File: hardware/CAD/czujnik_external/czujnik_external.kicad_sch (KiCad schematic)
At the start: 4 parts, among them J1 8P8C, J2 PMS5003 socket, J3 DHT22 socket, J4 ADC socket

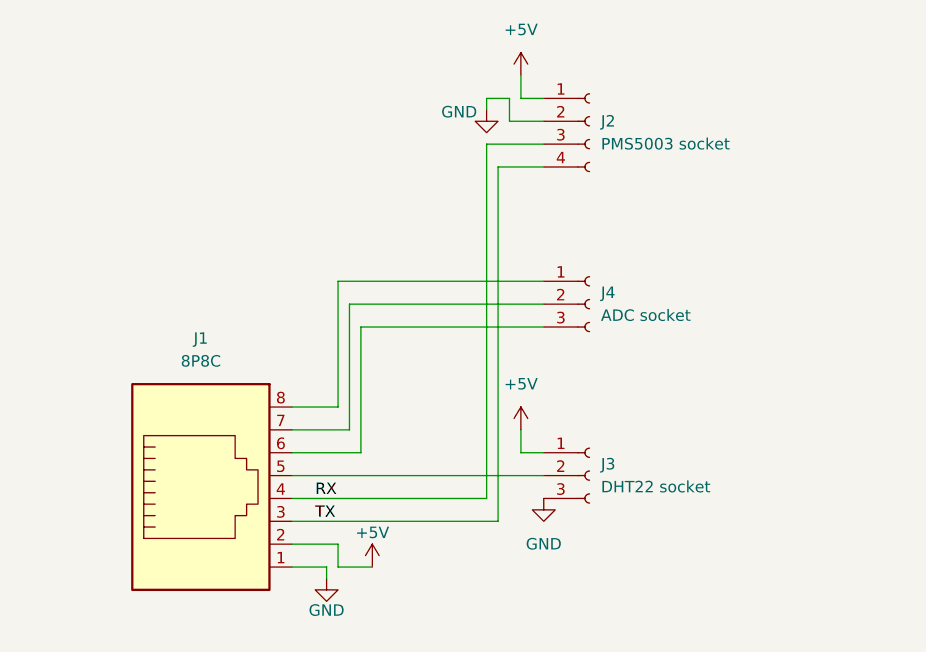
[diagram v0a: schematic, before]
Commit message: refactor PCBs, add gerber files
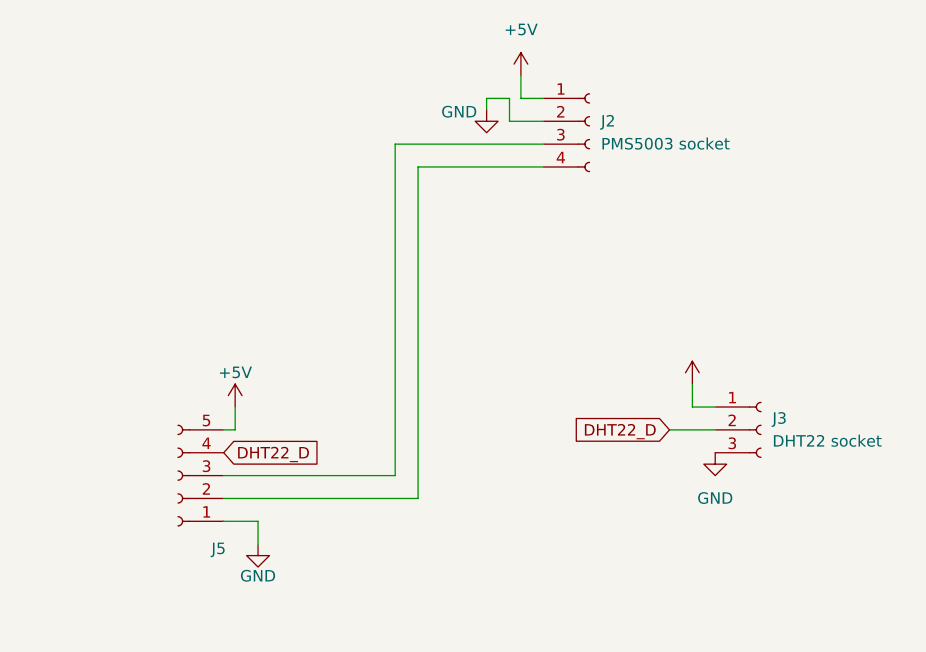
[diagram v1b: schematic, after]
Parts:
- removed J1: 8P8C, Connector_RJ:RJ45_Connfly_DS1128-09-S8xx-S_Horizontal, symbol Connector:8P8C
- removed J4: ADC socket, Connector_PinSocket_2.54mm:PinSocket_1x03_P2.54mm_Vertical, symbol Connector:Conn_01x03_Socket
- added J5: Conn_01x05_Socket, Connector_PinSocket_2.54mm:PinSocket_1x05_P2.54mm_Vertical, symbol Connector:Conn_01x05_Socket
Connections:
- net +5V: now also J5.5 (Pin_5)
- net GND: now also J5.1 (Pin_1)
- net DHT22_D: now reaches J3.2 (Pin_2)
- net DHT22_D: now also J5.4 (Pin_4)
- net RX: no longer names the net of J2.3 (Pin_3)
- net RX: now also J5.3 (Pin_3)
- net TX: no longer names the net of J2.4 (Pin_4)
- net TX: now also J5.2 (Pin_2)
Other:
- moved on the sheet: J3

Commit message: add DB9 connectors to PCBs
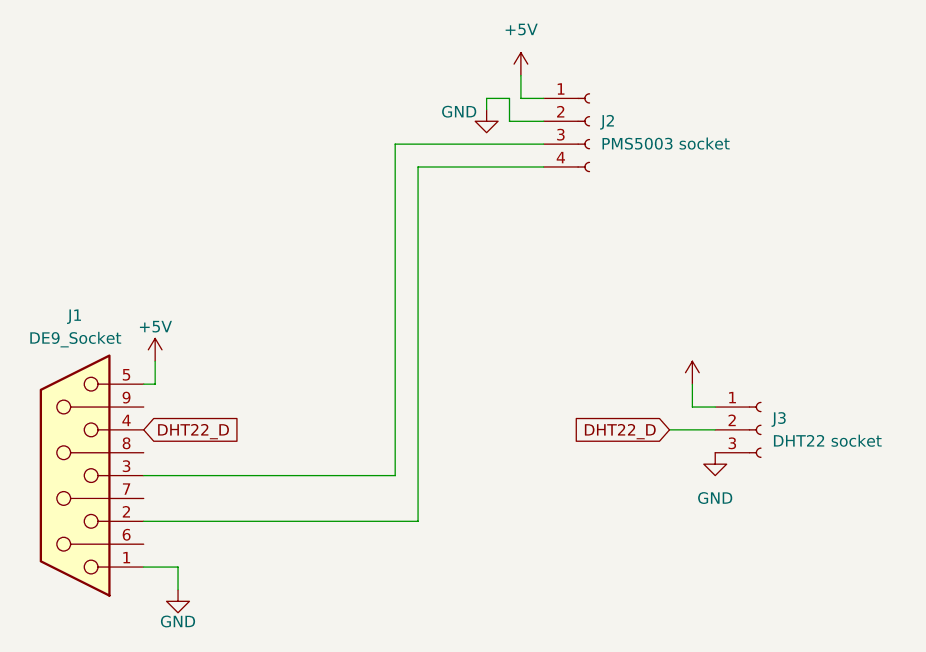
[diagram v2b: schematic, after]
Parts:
- removed J5: Conn_01x05_Socket, Connector_PinSocket_2.54mm:PinSocket_1x05_P2.54mm_Vertical, symbol Connector:Conn_01x05_Socket
- added J1: DE9_Socket, Connector_Dsub:DSUB-9_Socket_Horizontal_P2.77x2.54mm_EdgePinOffset9.40mm, symbol Connector:DE9_Socket
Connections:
- net +5V: now also J1.5
- net DHT22_D: now also J1.4
- net GND: now also J1.1
- net at J2.3 (Pin_3): now also J1.3
- net at J2.4 (Pin_4): now also J1.2
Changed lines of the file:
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@@
 	(wire
 		(pts
-			(xy 154.94 77.47) (xy 154.94 80.01)
-		)
-		(stroke
-			(width 0)
-			(type default)
-		)
-	)
-	(wire
-		(pts
-			(xy 151.13 74.93) (xy 172.72 74.93)
+			(xy 146.05 82.55) (xy 146.05 85.09)
+		)
+		(stroke
+			(width 0)
+			(type default)
+		)
+	)
+	(wire
+		(pts
+			(xy 142.24 72.39) (xy 170.18 72.39)
 		)
 		(stroke
@@
 	(wire
 		(pts
+			(xy 172.72 77.47) (xy 142.24 77.47)
+		)
+		(stroke
+			(width 0)
+			(type default)
+		)
+	)
+	(wire
+		(pts
 			(xy 182.88 30.48) (xy 180.34 30.48)
 		)
@@
 	(wire
 		(pts
-			(xy 152.4 67.31) (xy 151.13 67.31)
+			(xy 143.51 62.23) (xy 142.24 62.23)
 		)
 		(stroke
@@
 	(wire
 		(pts
-			(xy 151.13 77.47) (xy 154.94 77.47)
+			(xy 142.24 82.55) (xy 146.05 82.55)
 		)
 		(stroke
@@
 	(wire
 		(pts
-			(xy 172.72 74.93) (xy 172.72 38.1)
+			(xy 172.72 38.1) (xy 172.72 77.47)
 		)
 		(stroke
@@
 	(wire
 		(pts
-			(xy 152.4 64.77) (xy 152.4 67.31)
+			(xy 143.51 59.69) (xy 143.51 62.23)
 		)
 		(stroke
@@
 		(pts
 			(xy 186.69 30.48) (xy 184.15 30.48)
-		)
-		(stroke
-			(width 0)
-			(type default)
-		)
-	)
-	(wire
-		(pts
-			(xy 170.18 72.39) (xy 151.13 72.39)
 		)
 		(stroke
@@
 	(global_label "DHT22_D"
 		(shape input)
-		(at 151.13 69.85 0)
+		(at 142.24 67.31 0)
 		(fields_autoplaced yes)
 		(effects
@@
 		)
 		(property "Intersheetrefs" "${INTERSHEET_REFS}"
-			(at 162.3399 69.85 0)
+			(at 153.4499 67.31 0)
 			(effects
 				(font
@@
 		)
 		(property "Netclass" ""
-			(at 151.13 72.0408 0)
+			(at 142.24 69.5008 0)
 			(effects
 				(font
@@
 	)
 	(symbol
-		(lib_id "Connector:Conn_01x05_Socket")
-		(at 146.05 72.39 180)
-		(unit 1)
-		(exclude_from_sim no)
-		(in_bom yes)
-		(on_board yes)
-		(dnp no)
-		(property "Reference" "J5"
-			(at 151.384 80.518 0)
-			(effects
-				(font
-					(size 1.27 1.27)
-				)
-				(justify left)
-			)
-		)
-		(property "Value" "Conn_01x05_Socket"
-			(at 156.21 80.01 0)
-			(effects
-				(font
-					(size 1.27 1.27)
-				)
-				(justify left)
-				(hide yes)
-			)
-		)
-		(property "Footprint" "Connector_PinSocket_2.54mm:PinSocket_1x05_P2.54mm_Vertical"
-			(at 146.05 72.39 0)
-			(effects
-				(font
-					(size 1.27 1.27)
-				)
-				(hide yes)
-			)
-		)
-		(property "Datasheet" "~"
-			(at 146.05 72.39 0)
-			(effects
-				(font
-					(size 1.27 1.27)
-				)
-				(hide yes)
-			)
-		)
-		(property "Description" "Generic connector, single row, 01x05, script generated"
-			(at 146.05 72.39 0)
-			(effects
-				(font
-					(size 1.27 1.27)
-				)
-				(hide yes)
-			)
-		)
-		(pin "1"
-		)
-		(pin "3"
-		)
-		(pin "5"
-		)
-		(pin "2"
-		)
-		(pin "4"
-		)
-		(instances
-			(project ""
-				(path "/91a184b9-4010-4c25-ad3a-ff4cdc5d0b03"
-					(reference "J5")
-					(unit 1)
-				)
-			)
-		)
-	)
-	(symbol
 		(lib_id "power:+5V")
 		(at 203.2 62.23 0)
@@
 	(symbol
 		(lib_id "power:GND")
-		(at 154.94 80.01 0)
+		(at 146.05 85.09 0)
 		(unit 1)
 		(exclude_from_sim no)
@@
 		(dnp no)
 		(property "Reference" "#PWR01"
-			(at 154.94 86.36 0)
+			(at 146.05 91.44 0)
 			(effects
 				(font
@@
 		)
 		(property "Value" "GND"
-			(at 154.94 83.566 0)
+			(at 146.05 88.646 0)
 			(effects
 				(font
@@
 		)
 		(property "Footprint" ""
-			(at 154.94 80.01 0)
+			(at 146.05 85.09 0)
 			(effects
 				(font
@@
 		)
 		(property "Datasheet" ""
-			(at 154.94 80.01 0)
+			(at 146.05 85.09 0)
 			(effects
 				(font
@@
 		)
 		(property "Description" "Power symbol creates a global label with name \"GND\" , ground"
-			(at 154.94 80.01 0)
+			(at 146.05 85.09 0)
 			(effects
 				(font
@@
 				(path "/91a184b9-4010-4c25-ad3a-ff4cdc5d0b03"
 					(reference "#PWR01")
+					(unit 1)
+				)
+			)
+		)
+	)
+	(symbol
+		(lib_id "Connector:DE9_Socket")
+		(at 134.62 72.39 180)
+		(unit 1)
+		(exclude_from_sim no)
+		(in_bom yes)
+		(on_board yes)
+		(dnp no)
+		(fields_autoplaced yes)
+		(property "Reference" "J1"
+			(at 134.62 54.61 0)
+			(effects
+				(font
+					(size 1.27 1.27)
+				)
+			)
+		)
+		(property "Value" "DE9_Socket"
+			(at 134.62 57.15 0)
+			(effects
+				(font
+					(size 1.27 1.27)
+				)
+			)
+		)
+		(property "Footprint" "Connector_Dsub:DSUB-9_Socket_Horizontal_P2.77x2.54mm_EdgePinOffset9.40mm"
+			(at 134.62 72.39 0)
+			(effects
+				(font
+					(size 1.27 1.27)
+				)
+				(hide yes)
+			)
+		)
+		(property "Datasheet" "~"
+			(at 134.62 72.39 0)
+			(effects
+				(font
+					(size 1.27 1.27)
+				)
+				(hide yes)
+			)
+		)
+		(property "Description" "9-pin D-SUB connector, socket (female)"
+			(at 134.62 72.39 0)
+			(effects
+				(font
+					(size 1.27 1.27)
+				)
+				(hide yes)
+			)
+		)
+		(pin "8"
+		)
+		(pin "7"
+		)
+		(pin "1"
+		)
+		(pin "4"
+		)
+		(pin "5"
+		)
+		(pin "9"
+		)
+		(pin "6"
+		)
+		(pin "2"
+		)
+		(pin "3"
+		)
+		(instances
+			(project ""
+				(path "/91a184b9-4010-4c25-ad3a-ff4cdc5d0b03"
+					(reference "J1")
 					(unit 1)
 				)
@@
 	(symbol
 		(lib_id "power:+5V")
-		(at 152.4 64.77 0)
+		(at 143.51 59.69 0)
 		(unit 1)
 		(exclude_from_sim no)
@@
 		(dnp no)
 		(property "Reference" "#PWR02"
-			(at 152.4 68.58 0)
+			(at 143.51 63.5 0)
 			(effects
 				(font
@@
 		)
 		(property "Value" "+5V"
-			(at 152.4 60.96 0)
+			(at 143.51 55.88 0)
 			(effects
 				(font
@@
 		)
 		(property "Footprint" ""
-			(at 152.4 64.77 0)
+			(at 143.51 59.69 0)
 			(effects
 				(font
@@
 		)
 		(property "Datasheet" ""
-			(at 152.4 64.77 0)
+			(at 143.51 59.69 0)
 			(effects
 				(font
@@
 		)
 		(property "Description" "Power symbol creates a global label with name \"+5V\""
-			(at 152.4 64.77 0)
-			(effects
-				(font
+			(at 143.51 59.69 0)
+			(effects
+				(font
